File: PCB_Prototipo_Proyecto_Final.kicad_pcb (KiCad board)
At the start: 2 copper layers, 165.1 x 154.9 mm, 158 parts, among them IC1 UA741CP, J1 VIN, J10 Terminal_Sensores_Nivel, J11 Terminal_Sensor_Flujo, J12 Rele_4, J13 Rele_7, J14 Rele_1, J15 Rele_5, J16 Rele_2, J17 Rele_3, J18 Rele_6, J19 Pin_3V3, J2 Conn_01x15, J20 Conector 3V3, J21 Conector GND, J22 Pin_3V3, J23 Pin_3V3, J24 Pin GND, J25 Pin_3V3, J26 Pin GND, J27 Pin_3V3, J28 Pin_3V3, J29 Pin_3V3, J3 Conn_01x15, J30 Pin GND, J31 Pin GND, J32 Pin GND, J33 Pin GND, J34 Pin GND, J35 Pin GND, J36 Pin GND, J37 Pin GND, J38 Pin GND, J39 Pin GND, J4 Terminal_Sensor_pH, J40 Pin GND, J41 Pin GND, J42 Pin GND, J43 Conector GND, J44 Pin GND, J45 Pin_3V3, J46 Pin GND, J47 Pin GND, J5 Terminal_Sensor_CO2, J6 Terminal_Sensor_TDS, J7 Terminal_Sensor_Temp_Sumerg, J8 Terminal_Sensor_Iluminacion, J9 Terminal_Sensor_Temp_y_Hum, K1 SRD-05VDC-SL-C, K2 SRD-05VDC-SL-C, K3 SRD-05VDC-SL-C, K4 SRD-05VDC-SL-C, K5 SRD-05VDC-SL-C, K6 SRD-05VDC-SL-C, K7 SRD-05VDC-SL-C, Q1 2N7002, Q10 2N7002, Q11 2N7002, Q12 2N7002, Q13 2N7002, Q14 2N7002, Q15 2N7002, Q2 2N7002, Q3 2N7002, Q4 2N7002, Q5 2N7002, Q6 2N7002, Q7 2N7002, Q8 2N7002, Q9 2N7002, U1 LM2596S-ADJ, U2 LM1117-3.3, U3 MCP23008-xP

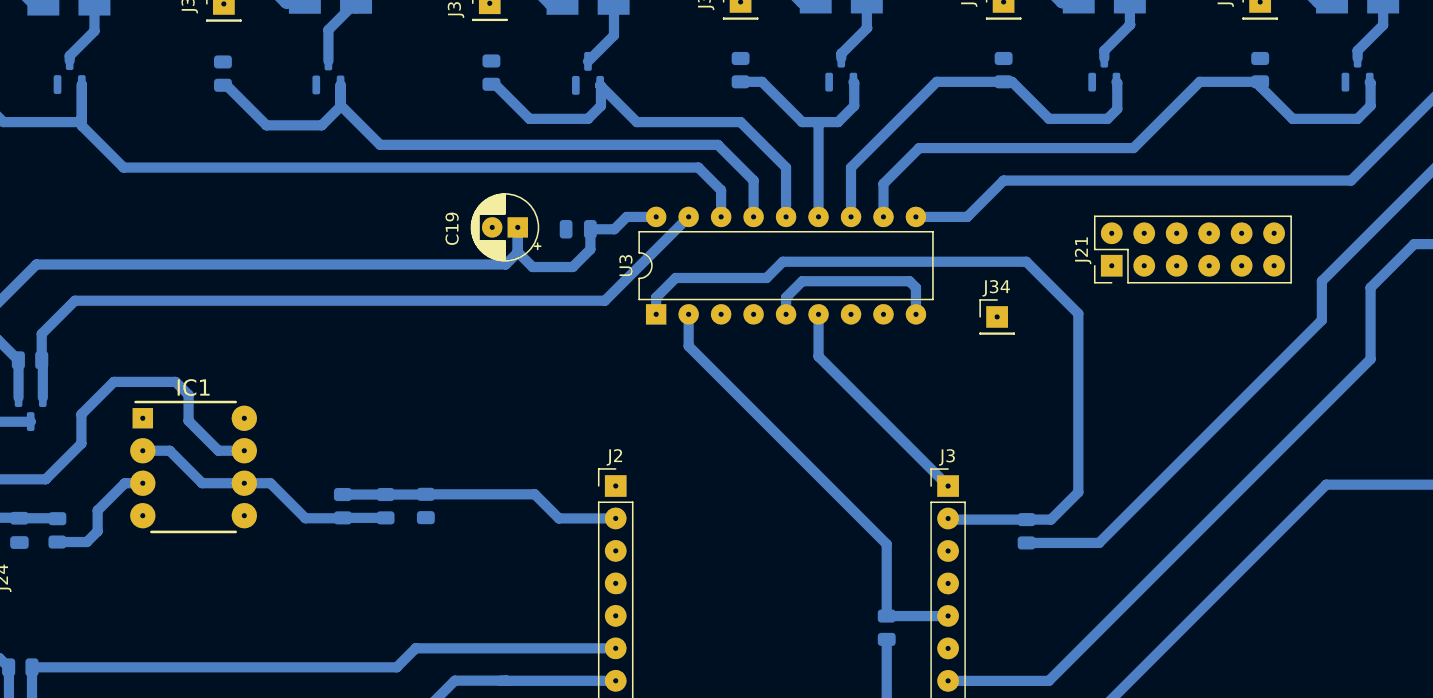
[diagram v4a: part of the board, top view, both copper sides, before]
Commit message: Modificación de footprint del MCP23008
Se lo modifico de forma de poder utilizar el adaptador SOP/PDIP, ya que tiene un ancho de 1,5 cm, que es más grande que el PDIP solo.
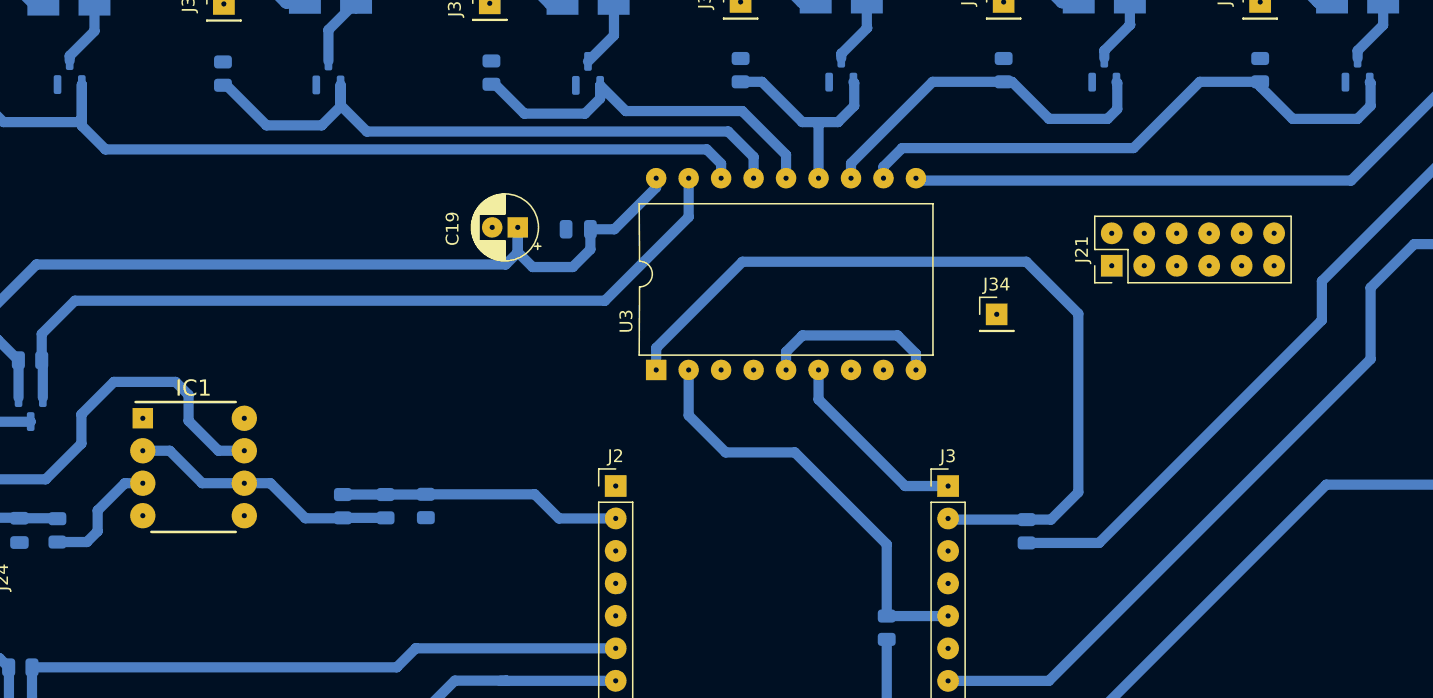
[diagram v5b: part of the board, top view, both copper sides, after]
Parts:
- moved U3 4.35 mm to (205.5, 117.4)
- moved J34 0.21 mm to (232.1, 113.1)
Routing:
- net /Microcontrolador/Rele_5: track 32.8 -> 29.6 mm
- net /Microcontrolador/Trigger__pH: track 59.4 -> 62.4 mm
- net /Microcontrolador/Rele_4: track 20.1 -> 17.1 mm
- net /Microcontrolador/Rele_3: track 31.1 -> 28.3 mm
- net /Microcontrolador/MCP23008_RESET: track 17.6 -> 15.2 mm
- net /Microcontrolador/Rele_2: track 47.7 -> 45.5 mm
- net /Microcontrolador/MCP23008_SCL: track 62.3 -> 64.3 mm
- net /Microcontrolador/Rele_7: track 70.1 -> 68.3 mm
- net /Microcontrolador/Rele_6: track 52.0 -> 50.2 mm
- net +3.3V: track 446.8 -> 448.4 mm
- net /Microcontrolador/MCP23008_SDA: track 34.8 -> 33.6 mm
- net /Microcontrolador/Rele_1: track 62.5 -> 61.4 mm

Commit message: Actualización de PCB y regeneración de Gerbers y Drill
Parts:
- moved C20 9.85 mm to (199.4, 96.6)
- moved D3 9.85 mm to (159.6, 79.0)
- moved D8 9.85 mm to (180.0, 78.8)
- moved J44 9.85 mm to (151.9, 79.0)
- moved K1 9.85 mm to (216.3, 65.3)
- moved K2 9.85 mm to (155.8, 65.0)
- moved Q10 9.85 mm to (159.6, 84.3)
- moved Q11 9.85 mm to (280.2, 84.1)
- moved Q13 9.85 mm to (260.4, 84.1)
- moved Q14 9.85 mm to (240.5, 84.1)
- moved Q15 9.85 mm to (179.8, 84.3)
- moved Q9 9.85 mm to (220.0, 84.1)
- moved R42 9.85 mm to (212.1, 84.1)
- moved R44 9.85 mm to (272.5, 84.1)
- moved R48 9.85 mm to (252.7, 84.1)
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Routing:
- net /Microcontrolador/MCP23008_SCL: track 64.3 -> 74.1 mm
- net +5V: track 612.2 -> 622.1 mm
- net /Microcontrolador/MCP23008_SDA: track 33.6 -> 43.5 mm
- net /Microcontrolador/MCP23008_RESET: track 15.2 -> 25.1 mm
- net +3.3V: track 448.4 -> 456.6 mm
- net /Microcontrolador/Trigger__pH: track 62.4 -> 66.8 mm
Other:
- board size 165.1 x 154.9 mm -> 165.1 x 164.9 mm
